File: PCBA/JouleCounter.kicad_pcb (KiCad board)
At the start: 4 copper layers, 42 x 49 mm, 87 parts, among them IC1001 L7983PU33R, IC901 MP4560DN-LF-Z, J101 JTAG, J501 USB_C_Receptacle, J502 USB_C_Receptacle, J601 USB_C_Receptacle, J901 Conn_02x25_Odd_Even_MountingP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, Q701 2N7002, Q702 MMBT3904, SW501 SW_DIP_x02, SW801 SW_Push, SW802 SW_Push, SW803 SW_Push, U201 BL706, U301 FUSB302B, U401 FUSB302B, U701 INA181, U702 TC2014-3.3VxCTTR, U901 LP2985-2.8, Y201 40MHz

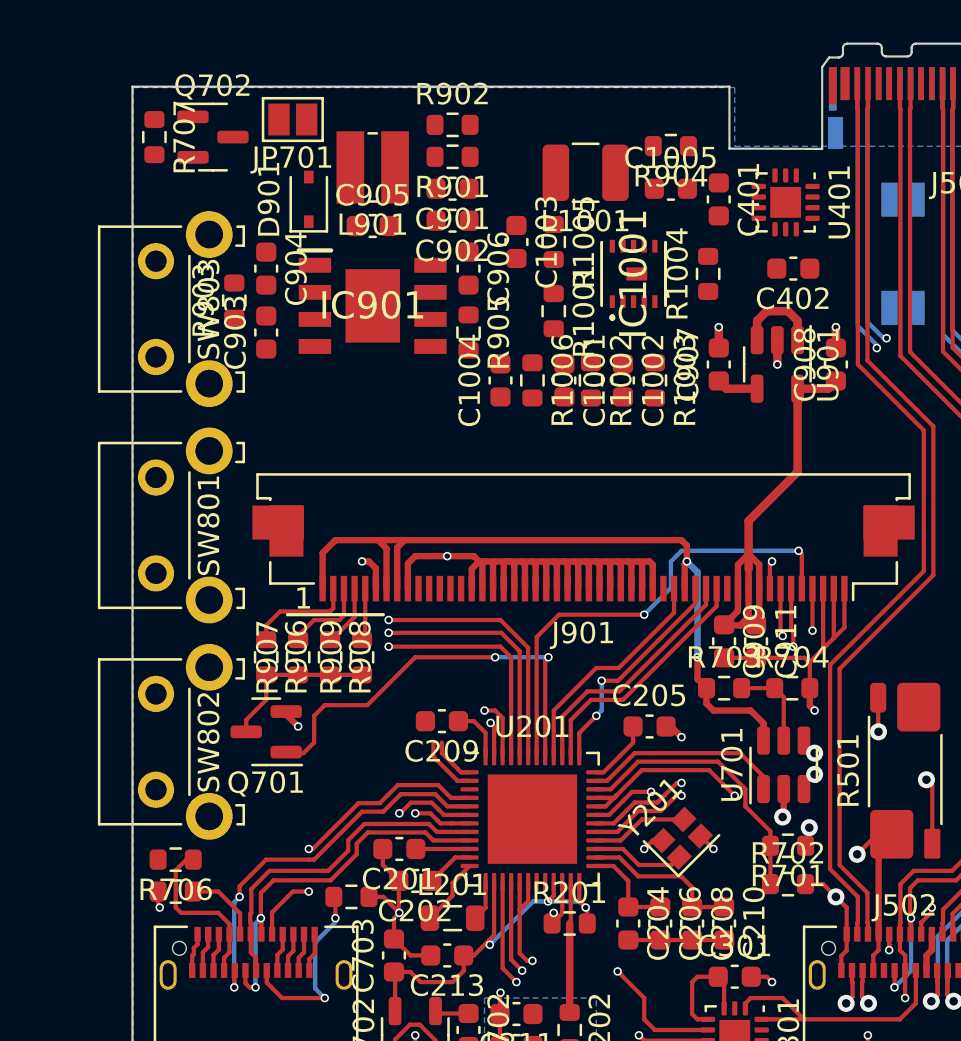
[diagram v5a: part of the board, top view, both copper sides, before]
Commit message: Step models for ports
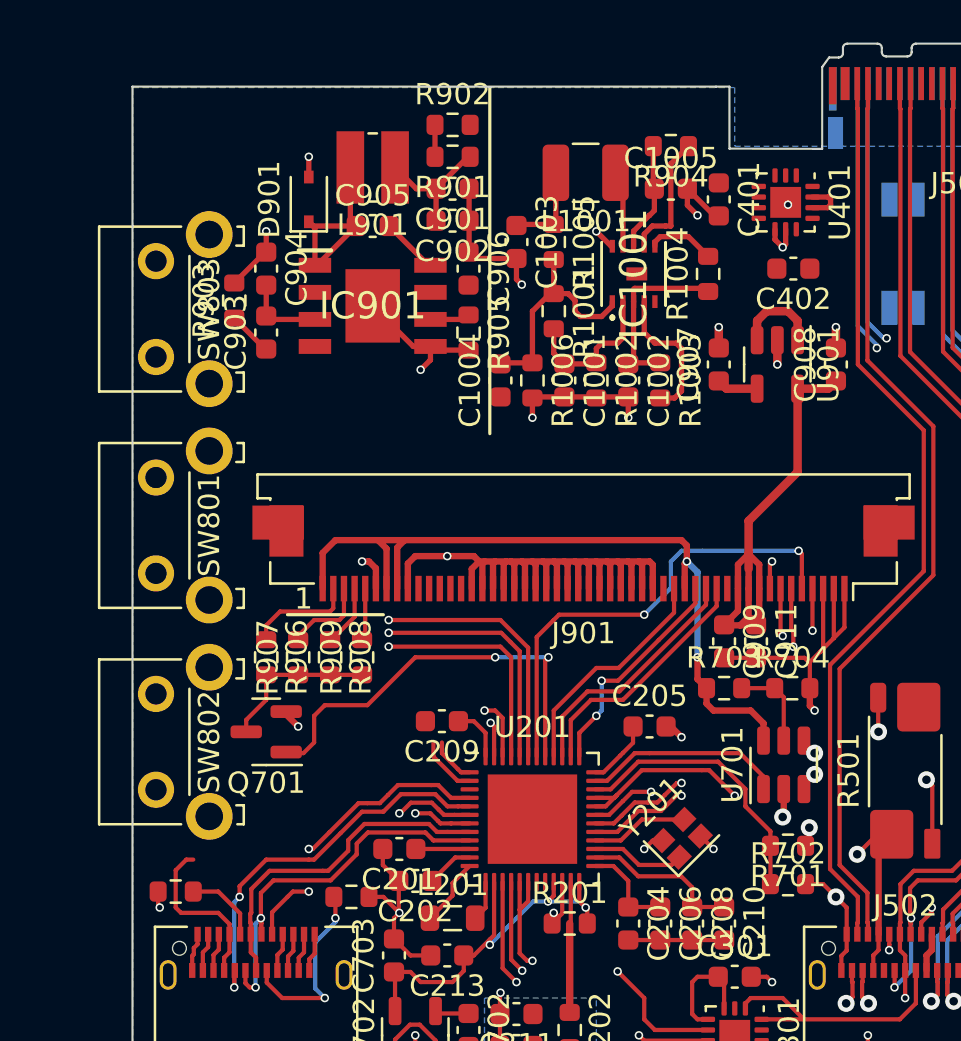
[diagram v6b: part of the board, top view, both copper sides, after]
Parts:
- removed JP701: Disable, Jumper:SolderJumper-2_P1.3mm_Open_Pad1.0x1.5mm
- removed Q702: MMBT3904, Package_TO_SOT_SMD:SOT-23
- removed R706: 100k, Resistor_SMD:R_0603_1608Metric
- removed R707: 1M, Resistor_SMD:R_0603_1608Metric
- moved C1002 0.25 mm to (217.5, 73.8)
- moved R1002 0.25 mm to (216.0, 73.8)
- moved R1003 0.25 mm to (219.0, 73.8)
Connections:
- C1003 pad 1: VDD -> /5V_USB
- C1004 pad 1: VDD -> /5V_USB
- C901 pad 2: VDD -> /5V_USB
- C902 pad 2: VDD -> /5V_USB
- L1001 pad 2: VDD -> /5V_USB
- L901 pad 1: VDD -> /5V_USB
- R1005 pad 1: VDD -> /5V_USB
- R901 pad 1: VDD -> /5V_USB
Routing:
- net GND: track 100.8 -> 131.2 mm, vias 20 -> 30
- net Net-(C1004-Pad2): track 0.00 -> 10.8 mm
- net /5V_USB: track 16.2 -> 26.5 mm
- net Net-(C905-Pad1): track 0.00 -> 10.0 mm
- net Net-(C1002-Pad1): track 0.00 -> 8.71 mm
- net Net-(C1001-Pad1): track 0.00 -> 7.21 mm
- net Net-(IC1001-Pad4): track 0.00 -> 6.65 mm
- net /Power/EN: track 0.00 -> 6.07 mm
- net /VBus: track 14.3 -> 19.4 mm
- net Net-(C903-Pad2): track 0.00 -> 3.80 mm
- net /Power/L7983/Lx: track 0.00 -> 3.59 mm
- net Net-(IC1001-Pad6): track 0.00 -> 3.19 mm
- net Net-(C905-Pad2): track 0.00 -> 2.70 mm
- net Net-(C903-Pad1): track 0.00 -> 2.10 mm
- net /FUSB302/VConn 5V: track 0.00 -> 2.05 mm
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
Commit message: PCB size
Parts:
- moved J601 9.99 mm to (199.5, 114.8)
- moved J502 9.97 mm to (230.5, 114.8)
- moved C203 3.47 mm to (175.0, 119.2)
- moved C207 3.47 mm to (174.0, 115.3)
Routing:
- net GND: track 131.2 -> 0.00 mm, vias 30 -> 0
- net /SENSE_USB_D+: track 71.9 -> 0.00 mm, vias 2 -> 0
- net VDD: track 71.5 -> 0.00 mm, vias 5 -> 0
- net /SENSE_USB_D-: track 70.4 -> 0.00 mm, vias 3 -> 0
- net /Measurement ports/RX1_+: track 48.6 -> 0.00 mm, vias 2 -> 0
- net /Measurement ports/RX1_-: track 48.6 -> 0.00 mm, vias 2 -> 0
- net /Measurement ports/TX2_-: track 47.1 -> 0.00 mm, vias 1 -> 0
- net /Measurement ports/TX2_+: track 47.1 -> 0.00 mm, vias 1 -> 0
- net /Measurement ports/TX1_+: track 43.6 -> 0.00 mm
- net /Measurement ports/TX1_-: track 43.6 -> 0.00 mm
- net /Measurement ports/RX2_+: track 41.9 -> 0.00 mm
- net /Measurement ports/RX2_-: track 41.9 -> 0.00 mm
- net /Button A: track 34.1 -> 0.00 mm, vias 1 -> 0
- net /5V_USB: track 26.5 -> 0.00 mm
- net /Button C: track 25.2 -> 0.00 mm, vias 1 -> 0
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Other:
- board size 42 x 49 mm -> 42.7 x 59.3 mm

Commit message: molex model
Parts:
- removed C907: C, Capacitor_SMD:C_0603_1608Metric
- removed R701: 1.4M, Resistor_SMD:R_0603_1608Metric
- removed R702, R703, R704: 100K, Resistor_SMD:R_0603_1608Metric
- U701: value INA181 -> INA226; footprint Package_TO_SOT_SMD:SOT-23-6 -> Package_SO:VSSOP-10_3x3mm_P0.5mm
- moved SW501 34.0 mm to (230.5, 101.8)
- moved U401 33.9 mm to (223.8, 99.2)
- moved C402 28.0 mm to (223.8, 96.5)
- moved U901 21.6 mm to (217.0, 93.2), turned to 90 degrees
- moved C908 19.6 mm to (218.0, 90.2), turned to 0 degrees
- moved R602 12.9 mm to (195.8, 107.5), turned to 0 degrees
- moved AE201 9.53 mm to (214.2, 117.5)
- moved C211 9.53 mm to (213.0, 113.0)
- moved C212 9.53 mm to (213.0, 114.5)
- moved R202 9.53 mm to (215.5, 113.8)
- moved SW802 9.28 mm to (195.2, 102.2)
- moved C204 9.28 mm to (216.8, 108.5)
- moved C206 9.28 mm to (218.2, 108.5)
- moved C208 9.28 mm to (219.8, 108.5)
- moved C210 9.28 mm to (221.2, 108.5)
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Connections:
- C302 pad 1: /FUSB303/VConn 5V -> /5V_USB
- C402 pad 1: /FUSB302/VConn 5V -> /5V_USB
- U201 pad 31: /Spare GPIO 0 -> /Main MCU/GPIO 16
- U201 pad 34: /VBus ADC -> /~{ADC IRQ}
- U201 pad 35: /Current ADC -> /Spare GPIO 0
- U301 pad 1: /CC2_X -> /CC1_X
- U301 pad 10: /CC1_X -> /CC2_X
- U301 pad 11: /CC1_X -> /CC2_X
- U301 pad 12: /FUSB303/VConn 5V -> /5V_USB
- U301 pad 13: /FUSB303/VConn 5V -> /5V_USB
- U301 pad 14: /CC2_X -> /CC1_X
- U401 pad 1: /CC2 -> /CC1
- U401 pad 10: /CC1 -> /CC2
- U401 pad 11: /CC1 -> /CC2
- U401 pad 12: /FUSB302/VConn 5V -> /5V_USB
- U401 pad 13: /FUSB302/VConn 5V -> /5V_USB
- U401 pad 14: /CC2 -> /CC1
- U701 pad 1: /Current ADC -> GND
- U701 pad 3: /I Sense 1 -> /~{ADC IRQ}
- U701 pad 4: /I Sense 2 -> /SDA
- U701 pad 5: /ADC Measurements/VRef -> /SCL
- U901 pad 4: Net-(C907-Pad1) -> unconnected-(U901-Pad4)
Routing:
- net GND: track 0.00 -> 68.7 mm, vias 0 -> 16
- net /Measurement ports/SBU2: track 0.00 -> 65.9 mm, vias 0 -> 2
- net /Measurement ports/RX1_-: track 0.00 -> 63.6 mm, vias 0 -> 1
- net /Measurement ports/RX1_+: track 0.00 -> 63.6 mm, vias 0 -> 1
- net /Measurement ports/TX1_-: track 0.00 -> 59.8 mm, vias 0 -> 2
- net /Measurement ports/TX1_+: track 0.00 -> 59.8 mm, vias 0 -> 2
- net /SENSE_USB_D+: track 0.00 -> 58.7 mm, vias 0 -> 2
- net /Measurement ports/TX2_-: track 0.00 -> 56.9 mm, vias 0 -> 1
- net /Measurement ports/TX2_+: track 0.00 -> 56.9 mm, vias 0 -> 1
- net /SENSE_USB_D-: track 0.00 -> 55.2 mm
- net /Measurement ports/SBU1: track 0.00 -> 53.5 mm
- net /Measurement ports/RX2_-: track 0.00 -> 52.4 mm
- net /Measurement ports/RX2_+: track 0.00 -> 52.4 mm
- net /CC1: track 0.00 -> 39.5 mm
- net /~{TOUCH_IRQ}: track 0.00 -> 27.5 mm, vias 0 -> 2
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- added copper zone on In2.Cu, net /Measurement ports/VBUS2
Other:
- outline, holes or cut-outs redrawn
